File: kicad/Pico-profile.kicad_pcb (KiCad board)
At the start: 2 copper layers, 32 parts, among them J1 Parallel, J2 DB25_Female, J3 Micro_SD_Card, J4 I2C, U1 74LS280, U2 74LS244, U3 74LVC244, U4 74LVC2G240, U5 74LVC1G04, U6 74LVC244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

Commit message: Intermediate commit. Worked on hardware
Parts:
- removed the R12 at (166.1, 34.3)
- removed the R9 at (154.1, 34.3)
- added R1: 0, Resistor_SMD:R_0603_1608Metric, F.Cu at (163.8, 71.2)
- added R11: 100, Resistor_SMD:R_0603_1608Metric, B.Cu at (149.1, 81.6)
- added R13: 100, Resistor_SMD:R_0603_1608Metric, B.Cu at (158.0, 81.6)
- added R14: 100, Resistor_SMD:R_0603_1608Metric, F.Cu at (180.7, 70.7)
- added R15: 100, Resistor_SMD:R_0603_1608Metric, F.Cu at (167.4, 71.4)
- added R16: 100, Resistor_SMD:R_0603_1608Metric, B.Cu at (125.0, 81.6)
- added R17: 100, Resistor_SMD:R_0603_1608Metric, F.Cu at (175.5, 62.7)
- added R18: 100, Resistor_SMD:R_0603_1608Metric, F.Cu at (175.3, 67.0)
- added U9: 74LVC1G04, Package_TO_SOT_SMD:SOT-23-5_HandSoldering, F.Cu at (180.6, 66.9)
- J3: footprint Connector_Card:microSD_HC_Hirose_DM3AT-SF-PEJM5 -> Connector_Card:microSD_HC_Molex_104031-0811
- R10: moved to B.Cu
- R12: renamed from R11; moved to B.Cu
- R6: renamed from R5; moved to B.Cu
- R7: renamed from R6; moved to B.Cu
- R8: renamed from R7; moved to B.Cu
- R9: renamed from R8; moved to B.Cu
- U2: footprint Package_SO:SOP-20_7.5x12.8mm_P1.27mm -> Package_SO:SOIC-20W_7.5x12.8mm_P1.27mm
- U3: footprint Package_SO:SOP-20_7.5x12.8mm_P1.27mm -> Package_SO:SOIC-20W_7.5x12.8mm_P1.27mm; moved to F.Cu
- U6: value 74LVC244 -> 74LVC1G04; footprint Package_SO:TSSOP-20_4.4x6.5mm_P0.65mm -> Package_TO_SOT_SMD:SOT-23-5_HandSoldering
- U8: moved to F.Cu
- moved U3 130.2 mm to (147.7, 116.7), turned to 270 degrees
- moved U5 129.0 mm to (125.4, 109.7)
- moved U2 114.5 mm to (147.7, 100.9), turned to 270 degrees
- moved U1 111.1 mm to (125.4, 97.8)
- moved C4 108.6 mm to (145.2, 139.5)
- moved C5 108.6 mm to (149.2, 139.5)
- moved J1 108.6 mm to (106.0, 75.6)
- moved R2 108.6 mm to (157.2, 140.3)
- moved R3 108.6 mm to (161.3, 140.3)
- moved R4 108.6 mm to (165.3, 140.3)
- moved U7 108.6 mm to (177.8, 101.0)
- moved J2 108.6 mm to (125.7, 66.7)
- moved R5 108.6 mm to (143.4, 142.8)
- moved C2 108.6 mm to (165.3, 137.8)
- moved C7 108.6 mm to (157.2, 137.4)
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- renumbered R1 to R2, R2 to R3, R3 to R4, R4 to R5
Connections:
- J1 pad 25: GND -> /PCHK
- J2 pad 25: GND -> /PCHK
- R10 pad 1: /PD5 -> /PD4
- R10 pad 2: /D5 -> /D4
- U2 pad 11: /OD4 -> /OD0
- U2 pad 12: /PD3 -> /PD1
- U2 pad 16: /PD1 -> /PD3
- U2 pad 18: /PD0 -> /PD4
- U2 pad 2: /OD0 -> /OD4
- U2 pad 4: /OD1 -> /OD3
- U2 pad 8: /OD3 -> /OD1
- U2 pad 9: /PD4 -> /PD0
- U3 pad 11: /PD4 -> /PD0
- U3 pad 12: /ID3 -> /ID1
- U3 pad 16: /ID1 -> /ID3
- U3 pad 18: /ID0 -> /ID4
- U3 pad 2: /PD0 -> /PD4
- U3 pad 4: /PD1 -> /PD3
- U3 pad 8: /PD3 -> /PD1
- U3 pad 9: /ID4 -> /ID0
- U4 pad 3: /~PBSY -> Net-(R15-Pad1)
- U4 pad 6: (no net) -> Net-(R14-Pad2)
- U5 pad 2: /PR~W -> Net-(R16-Pad2)
- U6 pad 1: GND -> (no net)
- U6 pad 2: /PR~W -> Net-(R17-Pad1)
- U6 pad 3: (no net) -> GND
- U6 pad 4: /~PCMD -> /CMD
- U6 pad 5: (no net) -> +3V3
- U7 pad 32: /~CMD -> /CMD
- U7 pad 34: /~STRB -> /STRB
- U8 pad 2: Net-(U6-Pad14) -> /~PRES
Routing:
- net /~PPARITY: track 0.00 -> 135.3 mm, vias 0 -> 1
- net /~PRES: track 0.00 -> 131.1 mm, vias 0 -> 2
- net /PCHK: track 0.00 -> 126.2 mm
- net /~PCMD: track 0.00 -> 120.9 mm, vias 0 -> 2
- net /~PSTRB: track 0.00 -> 116.1 mm, vias 0 -> 2
- net /~PBSY: track 0.00 -> 113.0 mm, vias 0 -> 2
- net /PD5: track 0.00 -> 88.2 mm, vias 0 -> 4
- net /PD7: track 0.00 -> 85.4 mm, vias 0 -> 4
- net /PD6: track 0.00 -> 83.2 mm, vias 0 -> 4
- net /D7: track 0.00 -> 83.2 mm
- net /PD4: track 0.00 -> 78.5 mm, vias 0 -> 2
- net /D4: track 0.00 -> 78.1 mm, vias 0 -> 1
- net /ID7: track 0.00 -> 77.3 mm
- net /ID5: track 0.00 -> 76.5 mm, vias 0 -> 2
- net /ID6: track 0.00 -> 75.3 mm, vias 0 -> 1
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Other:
- board outline added: 104 x 79 mm
- net class Default: clearance 0.2 -> 0.3; trace_width 0.25 -> 0.3; via_dia 0.8 -> 0.6; via_drill 0.4 -> 0.3
- net class Power added: clearance 0.3, trace_width 0.5, via_dia 0.6, via_drill 0.3
- rule trace_clearance: 0.2 -> 0.3
- rule trace_min: 0.2 -> 0.3
- rule via_min_size: 0.4 -> 0.6

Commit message: Hardware first revision. Need cosmetic changes
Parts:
- added D1: MBR1020VL, Diode_SMD:D_SOD-123F, F.Cu at (206.2, 63.1)
- added J5: Screw_Terminal_01x02, Connector_Phoenix_MSTB:PhoenixContact_MSTBA_2,5_2-G-5,08_1x02_P5.08mm_Horizontal, F.Cu at (212.0, 81.6)
- C2, C4, C5, C7, C8, R1, R14, R15, R17, R18, U4, U6, U8, U9: moved to B.Cu
- moved C5 80.6 mm to (192.2, 71.2), turned to 180 degrees
- moved J3 66.1 mm to (191.2, 126.4)
- moved C7 65.1 mm to (192.0, 82.3), turned to 180 degrees
- moved C2 46.8 mm to (126.0, 112.5), turned to 180 degrees
- moved C4 46.2 mm to (188.8, 124.3), turned to 270 degrees
- moved R2 43.9 mm to (199.8, 129.6), turned to 270 degrees
- moved R5 42.0 mm to (182.1, 126.5), turned to 180 degrees
- moved R3 41.8 mm to (199.8, 124.4), turned to 270 degrees
- moved U8 29.7 mm to (192.1, 85.4)
- moved R4 24.0 mm to (182.1, 123.1), turned to 180 degrees
- moved U7 22.6 mm to (191.9, 83.3)
- moved U6 20.1 mm to (192.1, 79.2)
- moved C8 19.1 mm to (192.2, 74.1)
- moved R14 16.9 mm to (163.9, 71.3)
- moved J4 16.7 mm to (170.5, 93.3)
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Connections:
- C2 pad 1: +5VL -> +3V3
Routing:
- net GND: track 21.2 -> 378.1 mm, vias 0 -> 18
- net +3V3: track 3.65 -> 250.8 mm, vias 0 -> 10
- net +5VL: track 0.00 -> 159.3 mm, vias 0 -> 5
- net /SD_CS: track 0.00 -> 57.7 mm
- net /ID7: track 77.3 -> 135.0 mm, vias 0 -> 3
- net /ID6: track 75.3 -> 132.3 mm
- net /SD_MOSI: track 0.00 -> 52.8 mm, vias 0 -> 2
- net /ID5: track 76.5 -> 128.1 mm, vias 2 -> 3
- net /RUN: track 58.6 -> 7.32 mm
- net /SD_MISO: track 0.00 -> 45.8 mm
- net /ID4: track 62.4 -> 108.0 mm, vias 2 -> 1
- net /~R~W: track 43.3 -> 86.5 mm
- net /ID3: track 62.7 -> 105.1 mm
- net /SD_SCK: track 0.00 -> 40.9 mm
- net /CMD: track 48.4 -> 7.82 mm
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- added copper zone on B.Cu, net GND
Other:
- board size 104 x 79 mm -> 124 x 79 mm
- net class Default: clearance 0.3 -> 0.25
- net class Power: clearance 0.3 -> 0.25; trace_width 0.5 -> 1
- rule trace_clearance: 0.3 -> 0.25

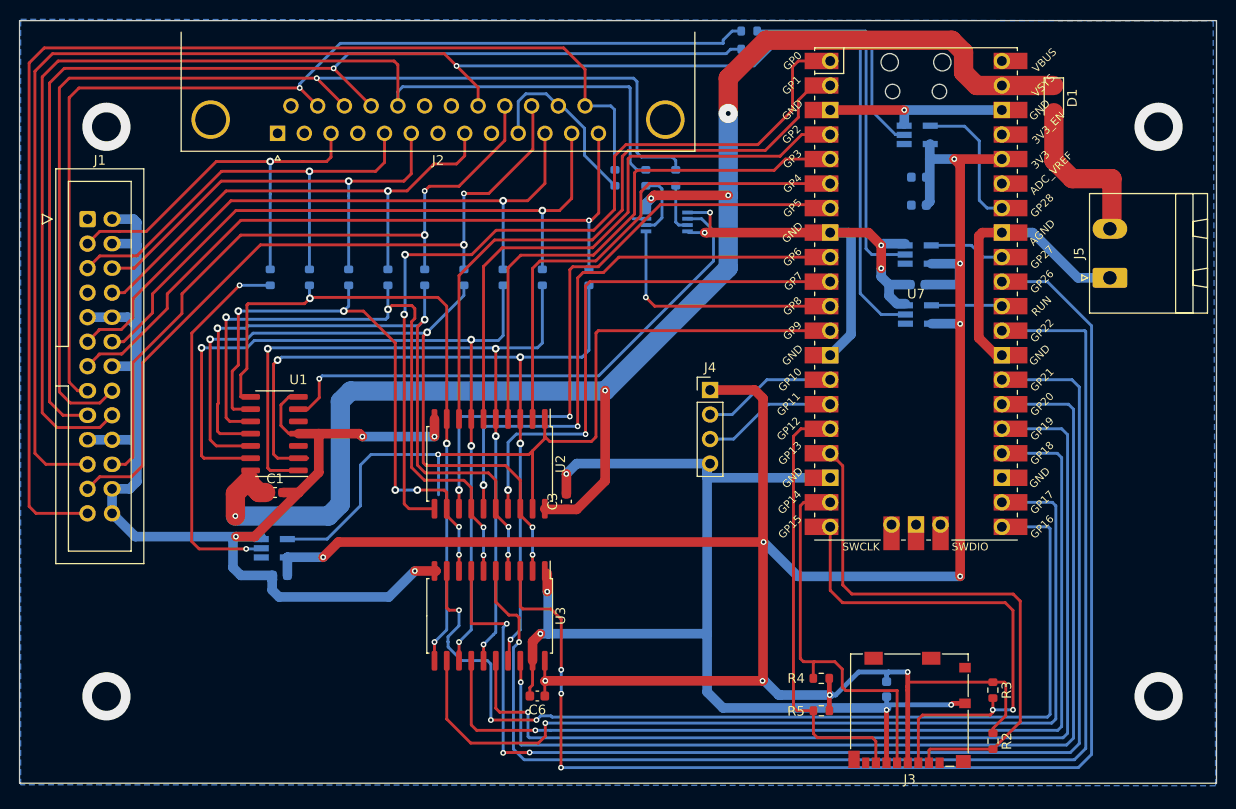
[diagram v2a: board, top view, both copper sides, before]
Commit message: Cosmetic changes on PCB
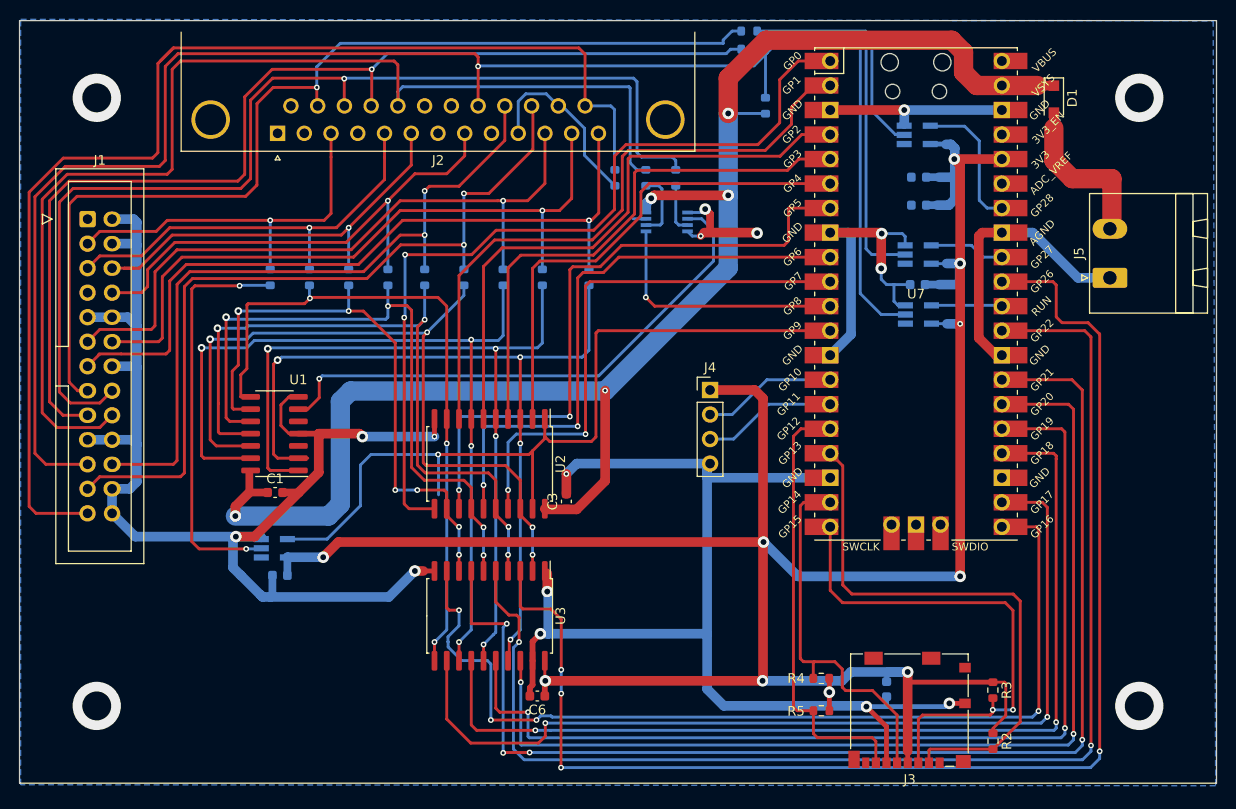
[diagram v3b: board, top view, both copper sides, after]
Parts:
- added R19: 10k, Resistor_SMD:R_0603_1608Metric, B.Cu at (176.3, 63.8)
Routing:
- net +3V3: track 250.8 -> 257.7 mm
- net /D4: track 77.4 -> 82.4 mm
- net /D0: track 48.5 -> 43.7 mm
- net /D1: track 48.4 -> 44.0 mm
- net +5VL: track 159.3 -> 163.4 mm
- net /~PCMD: track 116.1 -> 112.2 mm
- net /D3: track 71.4 -> 75.2 mm
- net /D7: track 73.8 -> 77.5 mm
- net GND: track 378.1 -> 374.7 mm, vias 18 -> 19
- net /ID7: track 135.0 -> 138.4 mm, vias 3 -> 4
- net /~PBSY: track 115.1 -> 111.7 mm
- net /D6: track 67.8 -> 70.5 mm
- net /PR~W: track 42.6 -> 39.9 mm
- net Net-(R16-Pad2): track 39.3 -> 42.0 mm
- net /ID0: track 103.1 -> 100.4 mm, vias 3 -> 4
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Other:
- net class Default: clearance 0.25 -> 0.3
- net class Power: clearance 0.25 -> 0.3; via_dia 0.6 -> 1.2; via_drill 0.3 -> 0.6
- rule trace_clearance: 0.25 -> 0.3
